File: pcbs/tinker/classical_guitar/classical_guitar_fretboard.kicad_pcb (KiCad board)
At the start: 2 copper layers, 188 parts, among them Q1 AO3401A, U1 AT42QT1110-A, U2 AT42QT1110-A, U3 AT42QT1110-A, U4 MP2359

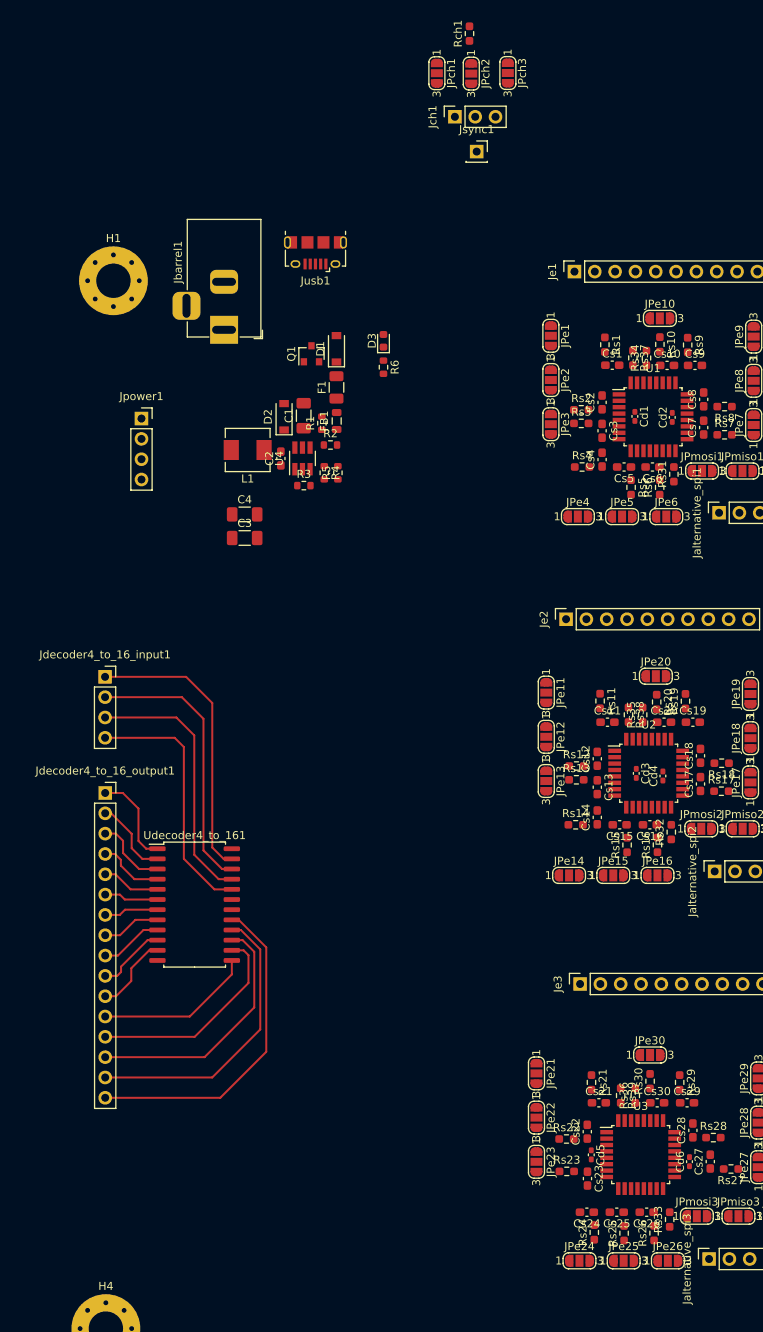
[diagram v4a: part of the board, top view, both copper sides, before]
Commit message: Rearranged jumpers for more efficient wiring
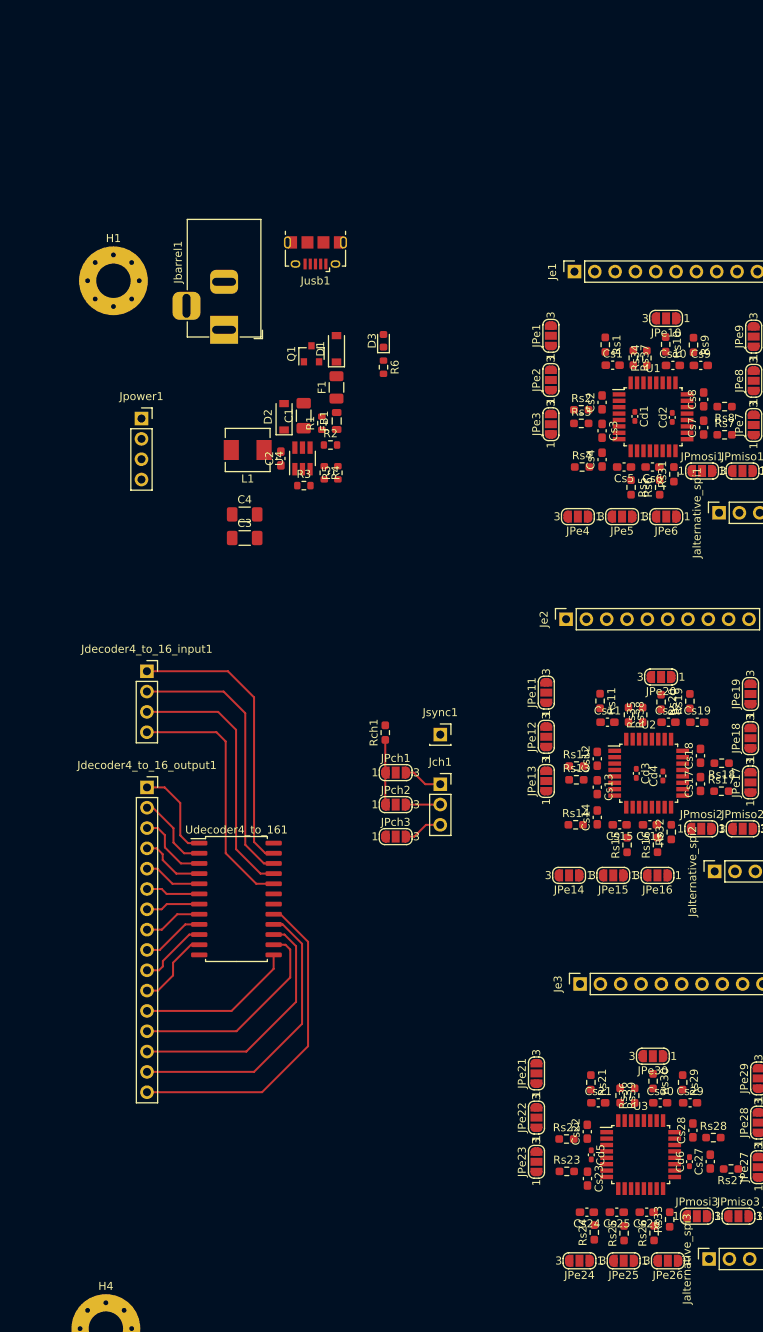
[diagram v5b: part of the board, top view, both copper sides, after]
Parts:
- moved JPch3 96.5 mm to (67.5, 90.5), turned to 0 degrees
- moved JPch2 91.9 mm to (67.5, 86.5), turned to 0 degrees
- moved Rch1 88.0 mm to (66.2, 77.5)
- moved JPch1 87.6 mm to (67.5, 82.5), turned to 0 degrees
- moved Jch1 83.4 mm to (73.0, 83.9), turned to 0 degrees
- moved Jsync1 73.0 mm to (73.0, 77.7)
- moved Jdecoder4_to_16_output1 5.27 mm to (36.4, 84.3)
- moved Jdecoder4_to_16_input1 5.27 mm to (36.4, 69.8)
- moved Udecoder4_to_161 5.27 mm to (47.6, 98.3)
- moved JPe10 0.78 mm to (101.3, 25.7), turned to 180 degrees
- moved Rs9 0.73 mm to (104.7, 29.0)
- moved Cs10 0.72 mm to (102.1, 31.6)
- moved Cs9 0.72 mm to (105.6, 31.6)
- moved Rs10 0.72 mm to (101.2, 28.9)
- moved JPe20 0.66 mm to (100.7, 70.5), turned to 180 degrees
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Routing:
- net Net-(JPch1-Pad1): track 0.00 -> 8.09 mm
- net Net-(JPch3-Pad3): track 0.00 -> 4.88 mm
- net Net-(JPch1-Pad3): track 0.00 -> 4.88 mm
- net Net-(JPch2-Pad3): track 0.00 -> 4.28 mm

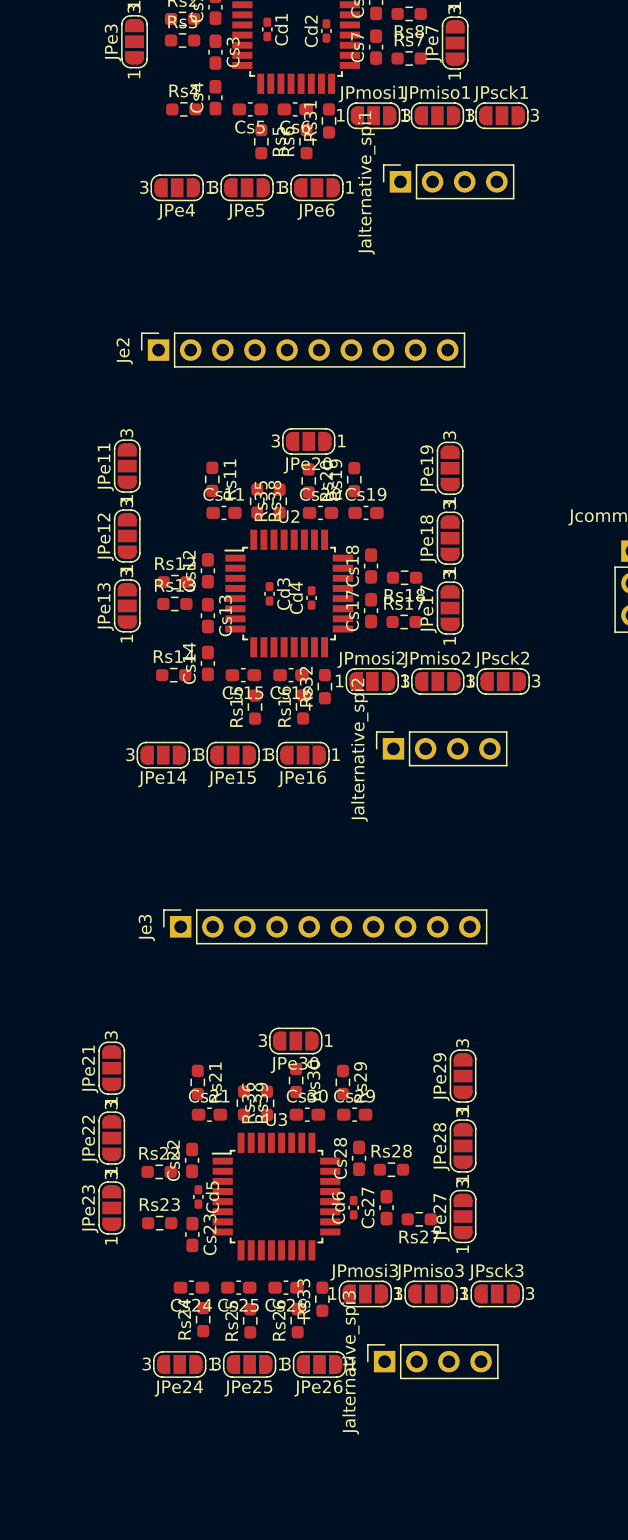
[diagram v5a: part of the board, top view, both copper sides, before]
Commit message: Completed tracing of second at42qt1110
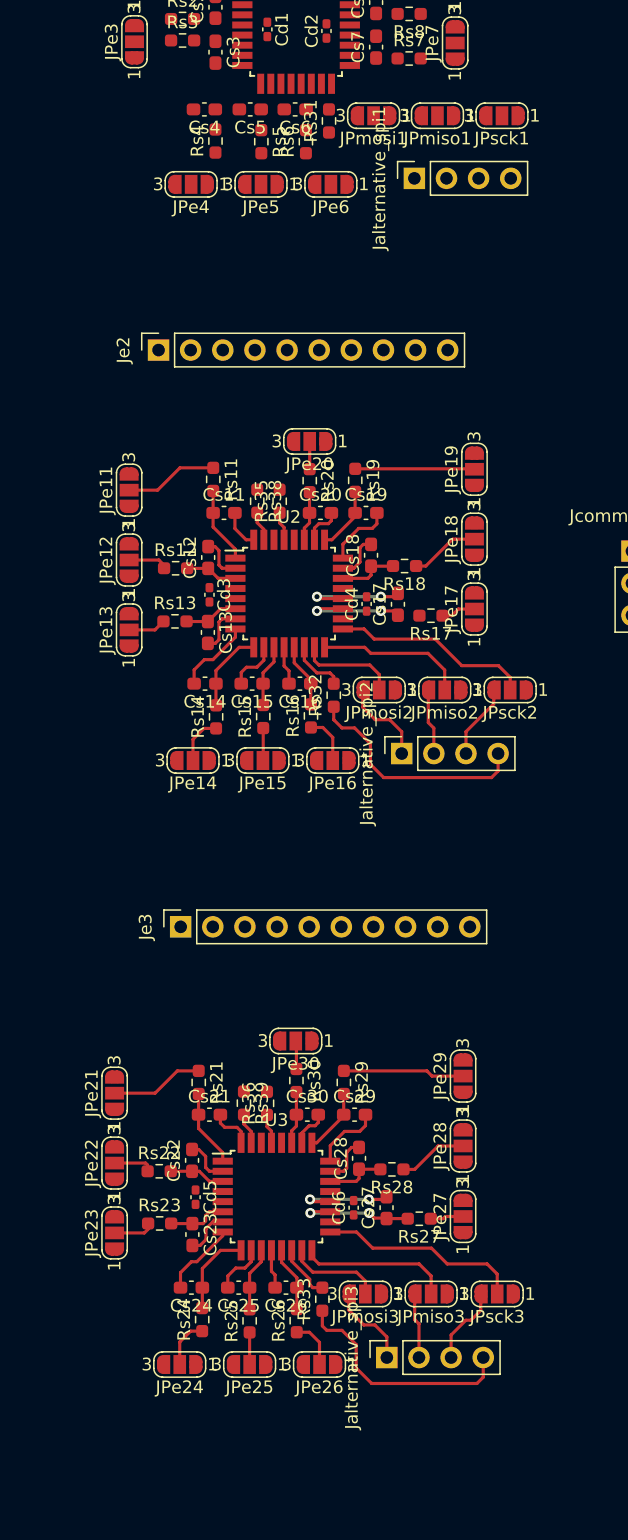
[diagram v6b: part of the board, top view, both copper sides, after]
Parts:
- moved Cd3 4.75 mm to (92.8, 82.7)
- moved Rs14 4.70 mm to (93.3, 92.3), turned to 90 degrees
- moved Cd4 4.38 mm to (105.2, 83.4)
- moved Rs4 3.54 mm to (93.3, 46.8), turned to 90 degrees
- moved JPe15 2.39 mm to (97.0, 95.8)
- moved JPe14 2.39 mm to (91.5, 95.8)
- moved JPe16 2.39 mm to (102.5, 95.8)
- moved Cs17 2.18 mm to (107.7, 83.4)
- moved Rs17 2.18 mm to (110.3, 84.3), turned to 180 degrees
- moved JPe22 1.99 mm to (85.3, 127.6)
- moved JPe21 1.99 mm to (85.3, 122.0)
- moved JPe23 1.99 mm to (85.3, 133.1)
- moved JPe17 1.93 mm to (113.8, 83.8)
- moved JPe18 1.93 mm to (113.8, 78.2)
- moved JPe19 1.93 mm to (113.8, 72.7)
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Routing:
- net Net-(Jalternative_spi3-Pad4): track 0.00 -> 18.6 mm
- net Net-(Jalternative_spi2-Pad4): track 0.00 -> 18.5 mm
- net /SCK3: track 0.00 -> 16.2 mm
- net /SCK2: track 0.00 -> 15.8 mm
- net /MISO2: track 0.00 -> 12.1 mm
- net /MISO3: track 0.00 -> 12.0 mm
- net /Electrode29: track 0.00 -> 9.60 mm
- net Net-(Cs27-Pad1): track 0.00 -> 9.50 mm, vias 0 -> 2
- net /Electrode19: track 0.00 -> 9.44 mm
- net Net-(Cs17-Pad1): track 0.00 -> 8.66 mm, vias 0 -> 2
- net Net-(Cs17-Pad2): track 0.00 -> 8.62 mm, vias 0 -> 2
- net /MOSI2: track 0.00 -> 7.86 mm
- net Net-(Cs27-Pad2): track 0.00 -> 7.81 mm, vias 0 -> 2
- net /MOSI3: track 0.00 -> 7.56 mm
- net /Electrode21: track 0.00 -> 7.38 mm
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
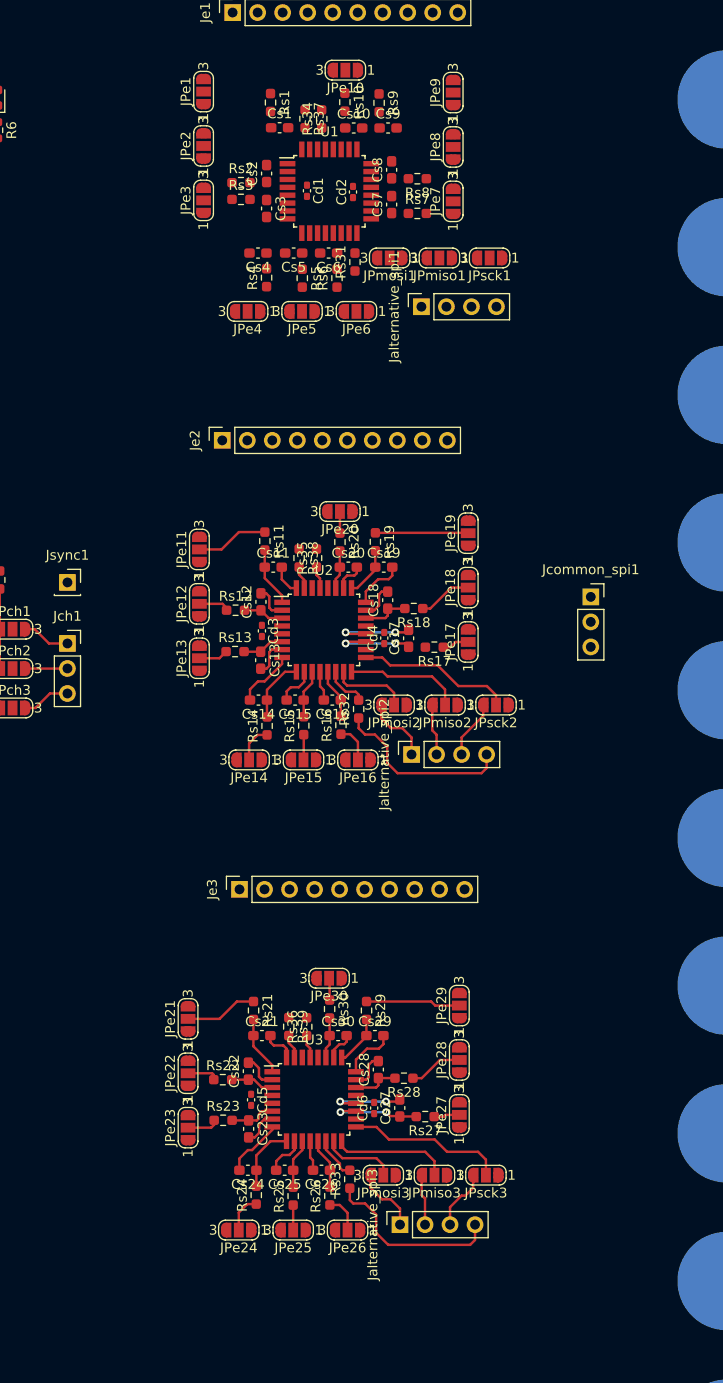
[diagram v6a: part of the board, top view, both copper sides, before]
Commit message: Testing electrode tracing
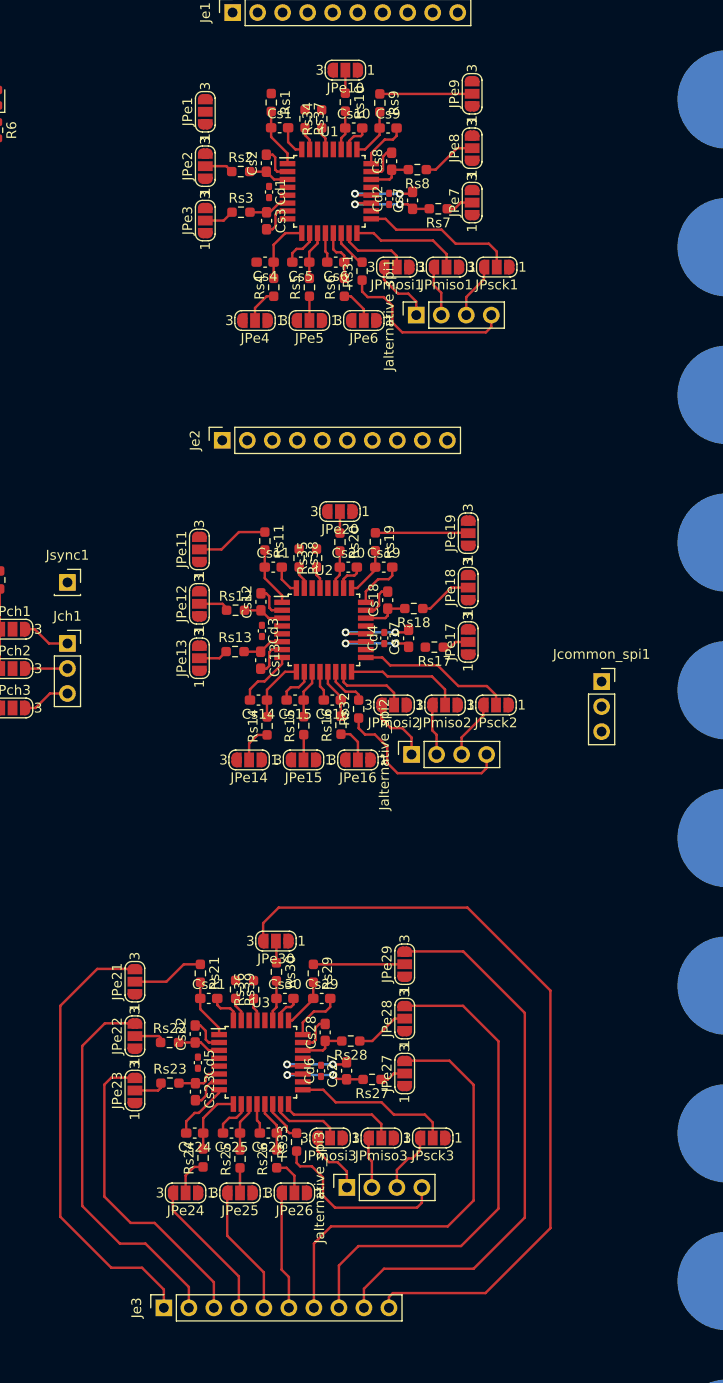
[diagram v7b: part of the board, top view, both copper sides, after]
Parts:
- moved Je3 43.2 mm to (82.8, 151.4)
- moved Jcommon_spi1 8.67 mm to (127.3, 87.8)
- moved JPe27 6.96 mm to (107.3, 127.6)
- moved JPe29 6.96 mm to (107.3, 116.5)
- moved JPe28 6.96 mm to (107.3, 122.0)
- moved Cd5 6.59 mm to (86.3, 126.5)
- moved Cs23 6.59 mm to (86.0, 129.4)
- moved Cs24 6.59 mm to (86.0, 133.7)
- moved Cs28 6.59 mm to (99.2, 123.4)
- moved Cs29 6.59 mm to (98.9, 120.0)
- moved JPe24 6.59 mm to (85.0, 139.7)
- moved JPe26 6.59 mm to (96.1, 139.7)
- moved JPmiso3 6.59 mm to (104.9, 134.2)
- moved JPmosi3 6.59 mm to (99.7, 134.2)
- moved Rs21 6.59 mm to (86.5, 117.4)
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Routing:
- net Net-(JPe30-Pad3): track 0.00 -> 79.7 mm
- net Net-(JPe29-Pad3): track 0.00 -> 56.8 mm
- net Net-(JPe28-Pad3): track 0.00 -> 50.9 mm
- net Net-(JPe21-Pad3): track 0.00 -> 46.0 mm
- net Net-(JPe27-Pad3): track 0.00 -> 44.3 mm
- net Net-(JPe22-Pad3): track 0.00 -> 38.9 mm
- net Net-(JPe23-Pad3): track 0.00 -> 32.1 mm
- net Net-(Jalternative_spi1-Pad4): track 0.00 -> 18.4 mm
- net /SCK1: track 0.00 -> 15.7 mm
- net Net-(JPe24-Pad3): track 0.00 -> 14.5 mm
- net Net-(JPe25-Pad3): track 0.00 -> 13.2 mm
- net Net-(JPe26-Pad3): track 0.00 -> 12.0 mm
- net /MISO1: track 0.00 -> 11.3 mm
- net Net-(Cs7-Pad1): track 0.00 -> 9.45 mm, vias 0 -> 2
- net /Electrode9: track 0.00 -> 9.38 mm
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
